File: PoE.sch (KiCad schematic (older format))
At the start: 25 parts, among them IC1 TPS2378DDA

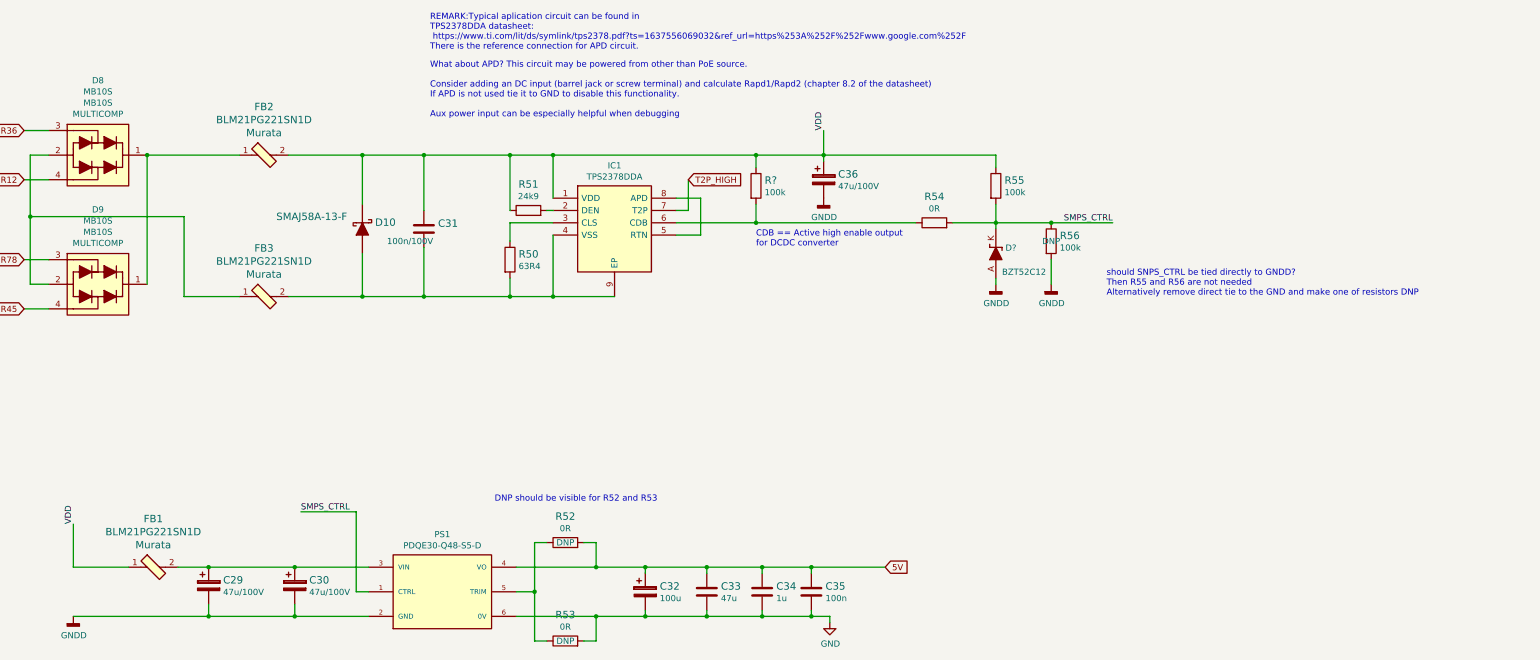
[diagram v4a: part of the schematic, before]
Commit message: added 7k5 resistor between rtn and vdd, removed transistor circuit, add descriptions
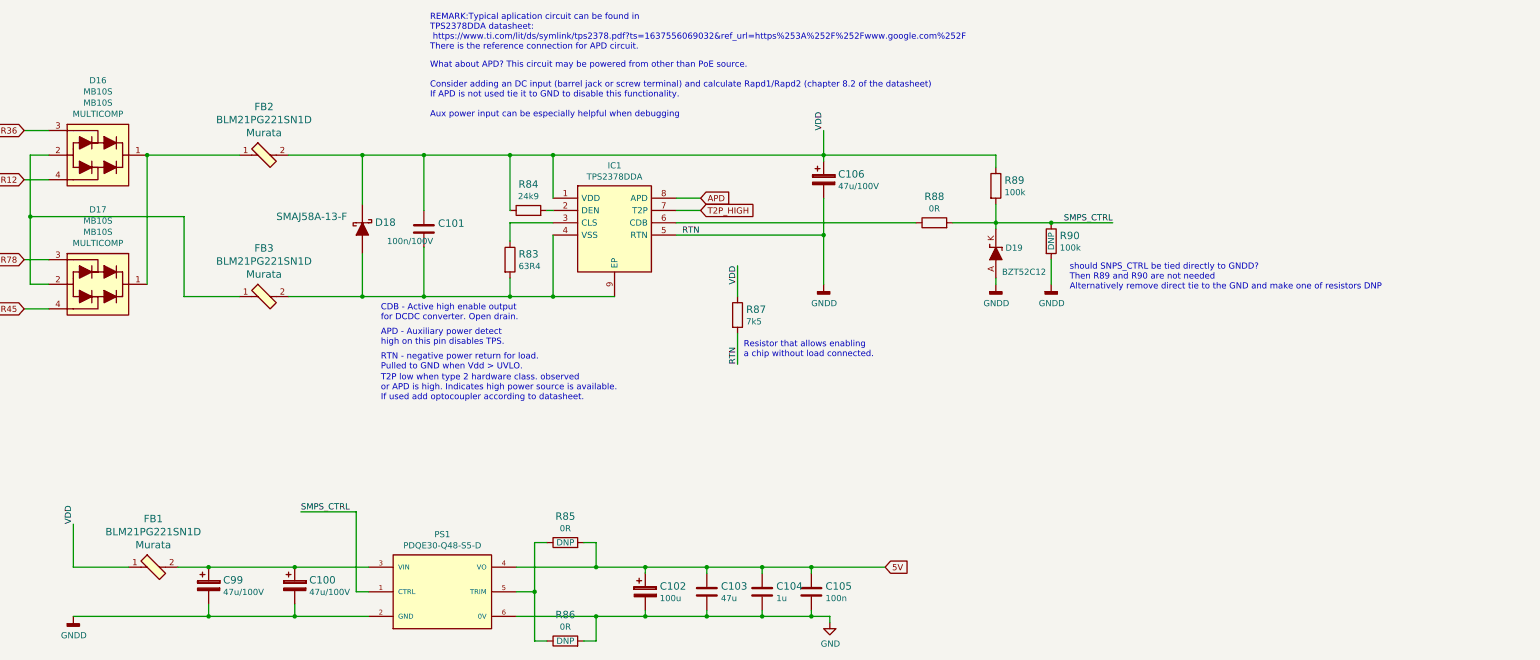
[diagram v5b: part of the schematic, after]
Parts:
- removed R?: R_100k_0402, antmicro-footprints:0402-res, symbol antmicroResistors0402:R_100k_0402
- added R87: R_7k5_2512, antmicro-footprints:2512-res, symbol antmicroResistorsmisc:R_7k5_2512
- gave numbers to parts that had none: 1
- renumbered C30 to C100, C31 to C101, C32 to C102, C33 to C103, C34 to C104, C35 to C105, C36 to C106, C29 to C99, D8 to D16, D9 to D17, D10 to D18, R50 to R83, R51 to R84, R52 to R85, R53 to R86, R54 to R88, R55 to R89, R56 to R90
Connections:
- net GNDD: now also IC1.5 (RTN), R87.2
- net VDD: now also R87.1
- net APD: now reaches IC1.8 (APD)
- net APD: no longer IC1.5 (RTN)
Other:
- note added: "APD - Auxiliary power detect \nhigh on this pin disables TPS."
- note added: "CDB - Active high enable output \nfor DCDC converter. Open drain."
- note added: "RTN - negative power return for load.\nPulled to GND when Vdd > UVLO."
- note added: "Resistor that allows enabling\na chip without load connected."
- note added: "T2P low when type 2 hardware class. observed\nor APD is high. Indicates high power source is available. \nIf used add optocoupler according to datasheet."
- note added: "should SNPS_CTRL be tied directly to GNDD?\nThen R89 and R90 are not needed\nAlternatively remove direct tie to the GND and make one of resistors DNP"
- note removed: "CDB == Active high enable output \nfor DCDC converter"
- note removed: "DNP should be visible for R52 and R53"
- note removed: "should SNPS_CTRL be tied directly to GNDD?\nThen R55 and R56 are not needed\nAlternatively remove direct tie to the GND and make one of resistors DNP"

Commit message: annotations
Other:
- moved on the sheet: C100, C102, C103, C104, C105, C99, FB1, PS1, R85, R86

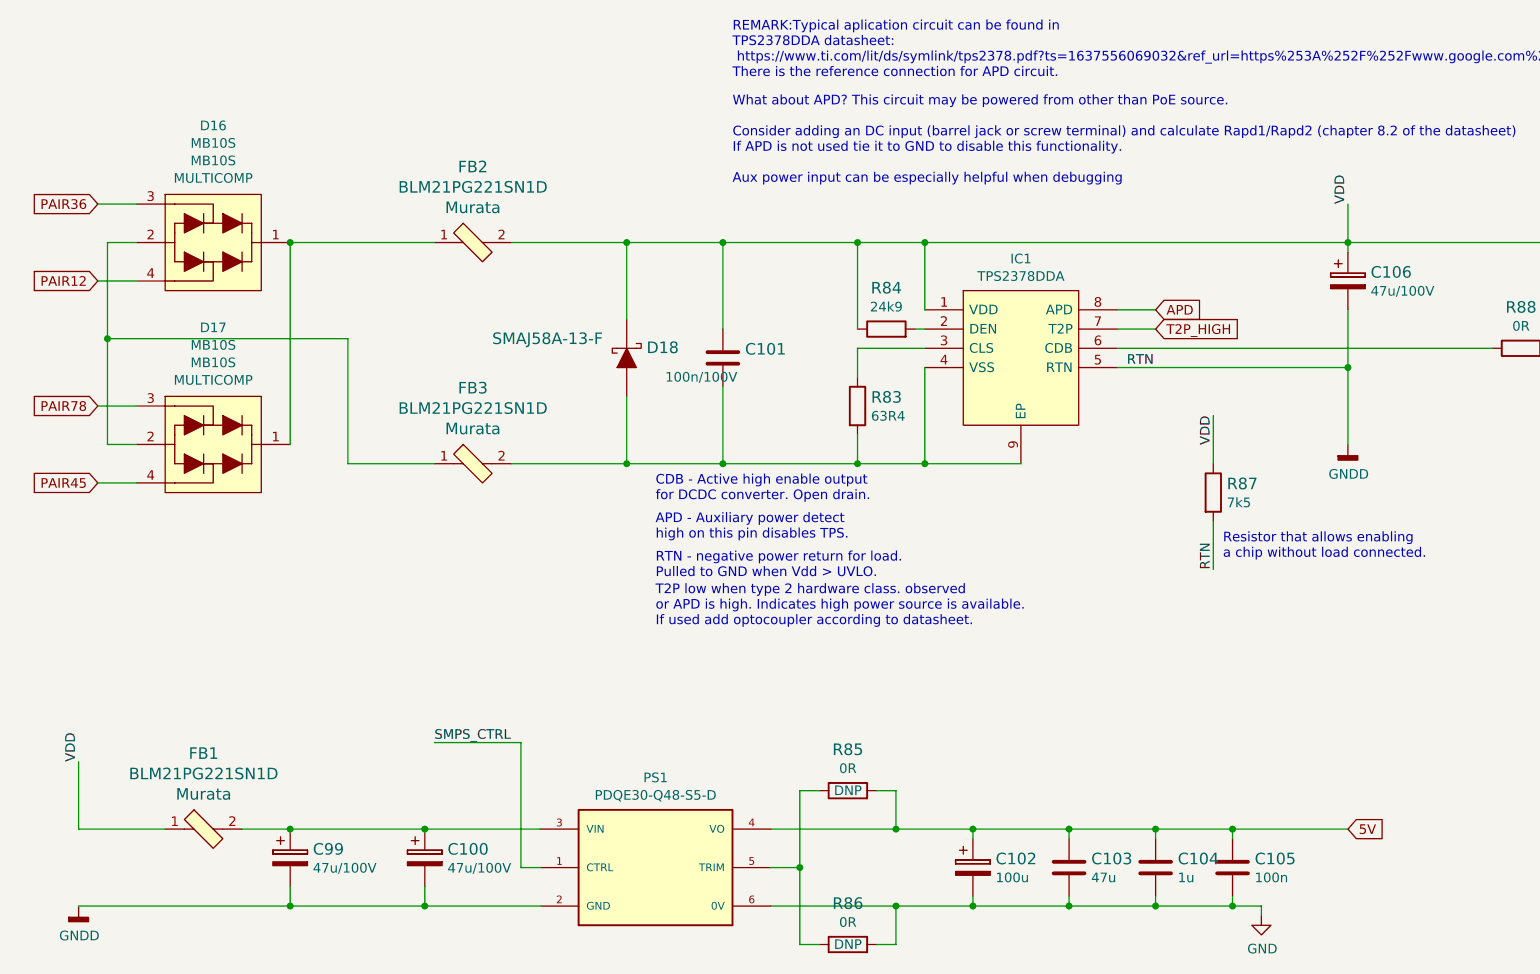
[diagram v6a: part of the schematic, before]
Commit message: changed naming convention for main powerline
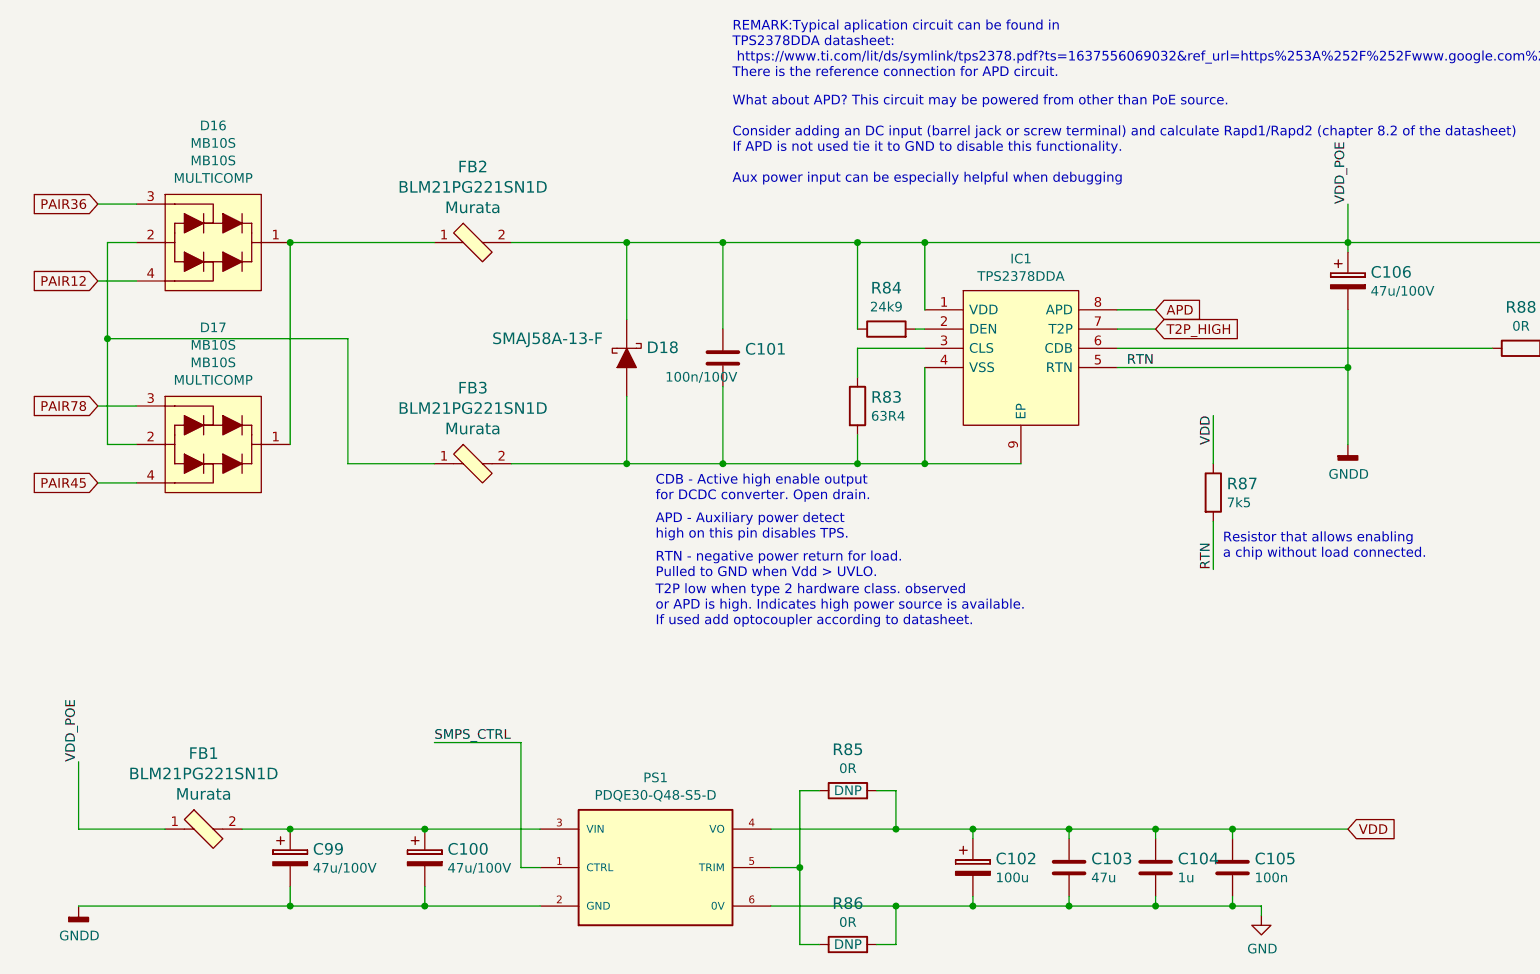
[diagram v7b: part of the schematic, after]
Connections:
- net 5V is gone; now on net VDD: C102.1, C103.1, C104.1, C105.1, PS1.4 (VO), R85.2
- net VDD: no longer C101.1, C106.1, D18.K, FB1.1, FB2.2, IC1.1 (VDD), R84.1, R89.1
- new net VDD_POE: C101.1, C106.1, D18.K, FB1.1, FB2.2, IC1.1 (VDD), R84.1, R89.1
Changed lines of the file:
@@
 Wire Wire Line
 	1350 5200 2450 5200
-Text GLabel 7950 4800 2    50   Input ~ 0
-5V
 Text Label 7950 1550 1    50   ~ 0
-VDD
+VDD_POE
 Text Label 1350 4450 1    50   ~ 0
-VDD
+VDD_POE
 Text Notes 9950 2850 0    50   ~ 0
 should SNPS_CTRL be tied directly to GNDD?\nThen R89 and R90 are not needed\nAlternatively remove direct tie to the GND and make one of resistors DNP
@@
 Text Label 7250 3450 1    50   ~ 0
 RTN
+Text GLabel 7950 4800 2    50   Input ~ 0
+VDD
 $EndSCHEMATC

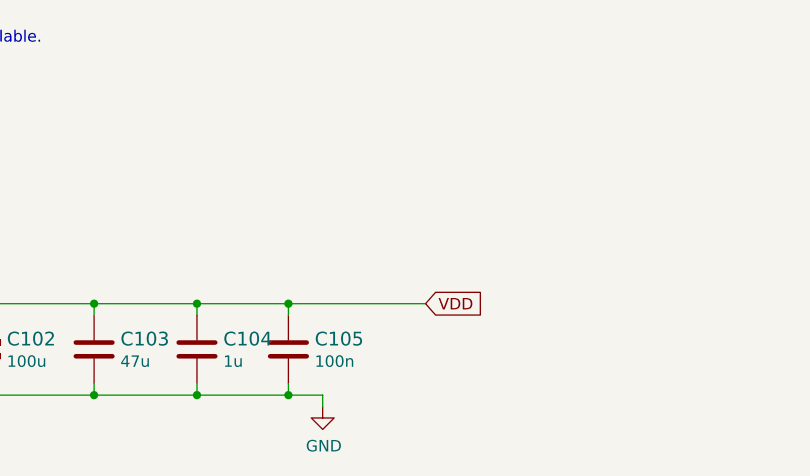
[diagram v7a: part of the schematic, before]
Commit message: add 5V psu logic
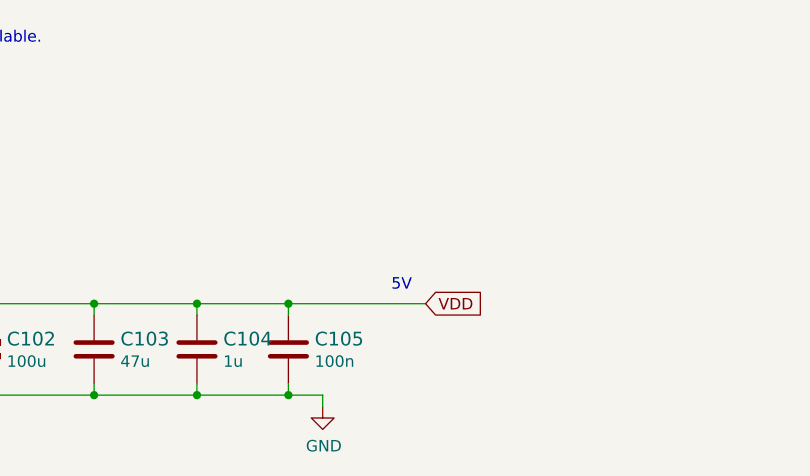
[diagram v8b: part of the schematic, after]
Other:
- note added: "5V"
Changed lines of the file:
@@
 Text GLabel 7950 4800 2    50   Input ~ 0
 VDD
+Text Notes 7800 4750 0    50   ~ 0
+5V
 $EndSCHEMATC
